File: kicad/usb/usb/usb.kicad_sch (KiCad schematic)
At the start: 17 parts, among them J1 USB_C_Receptacle_USB2.0_14P, J2 PH2.0mm 2P, J3 Conn_01x07_Pin, SW1 PWR, U1 S-T111B33MC-OGSTFU, U2 MCP73831-2-OT

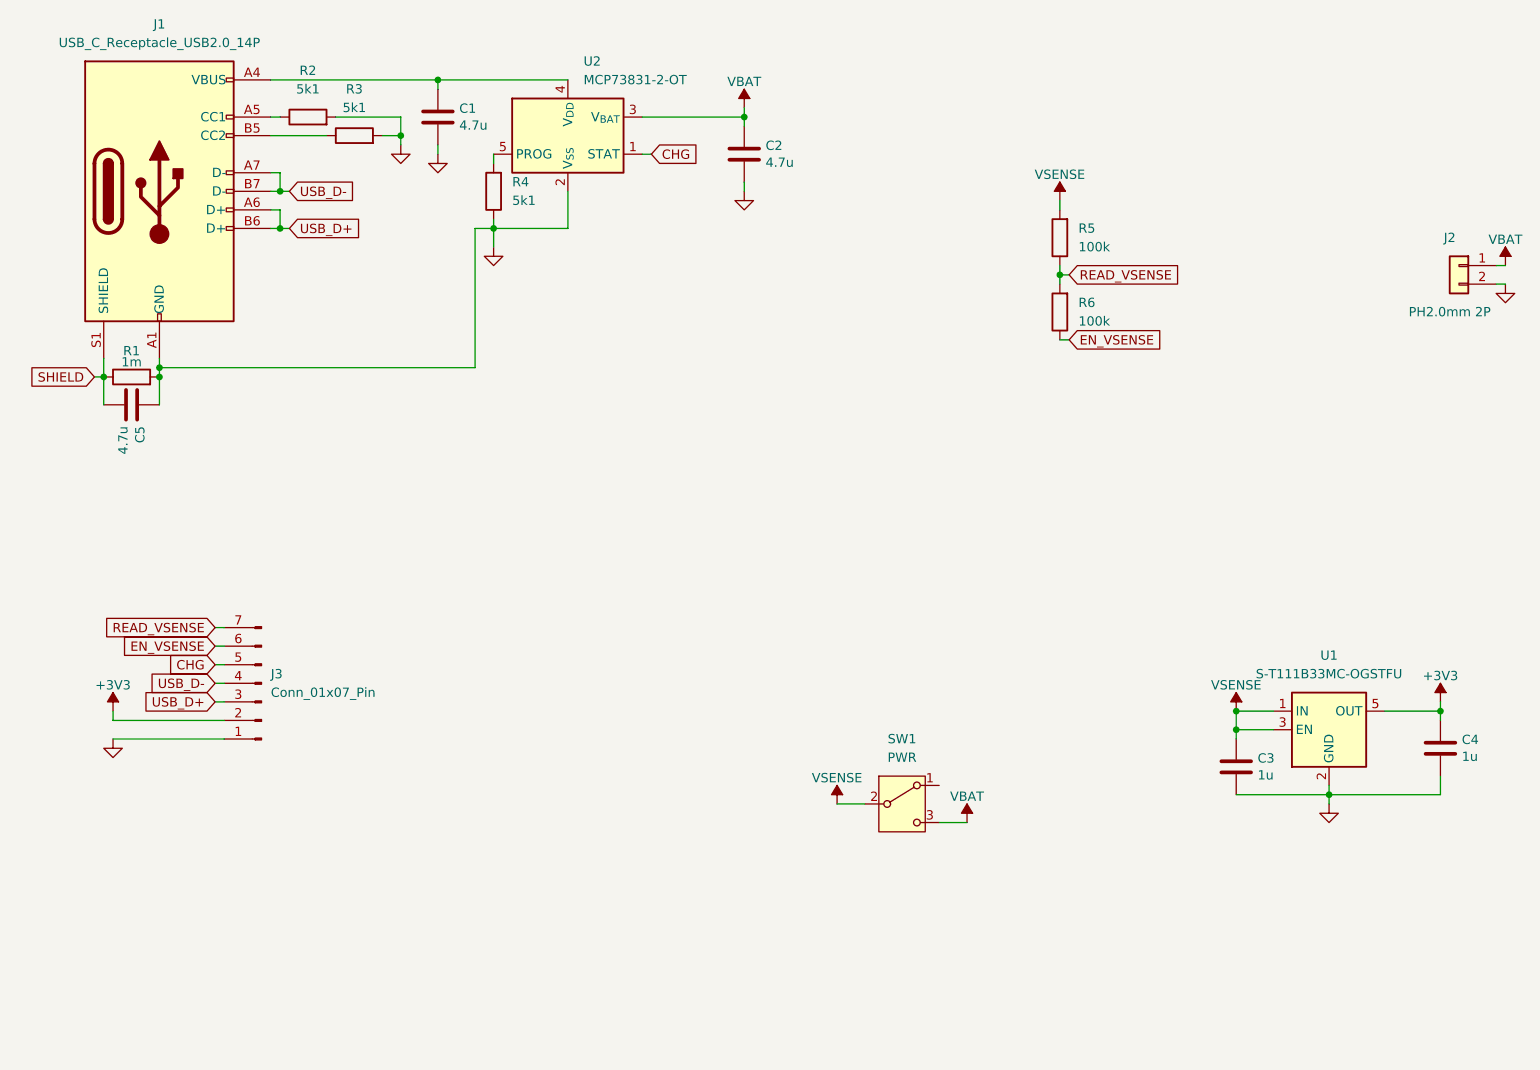
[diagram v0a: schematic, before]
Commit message: Working on usb fabrication
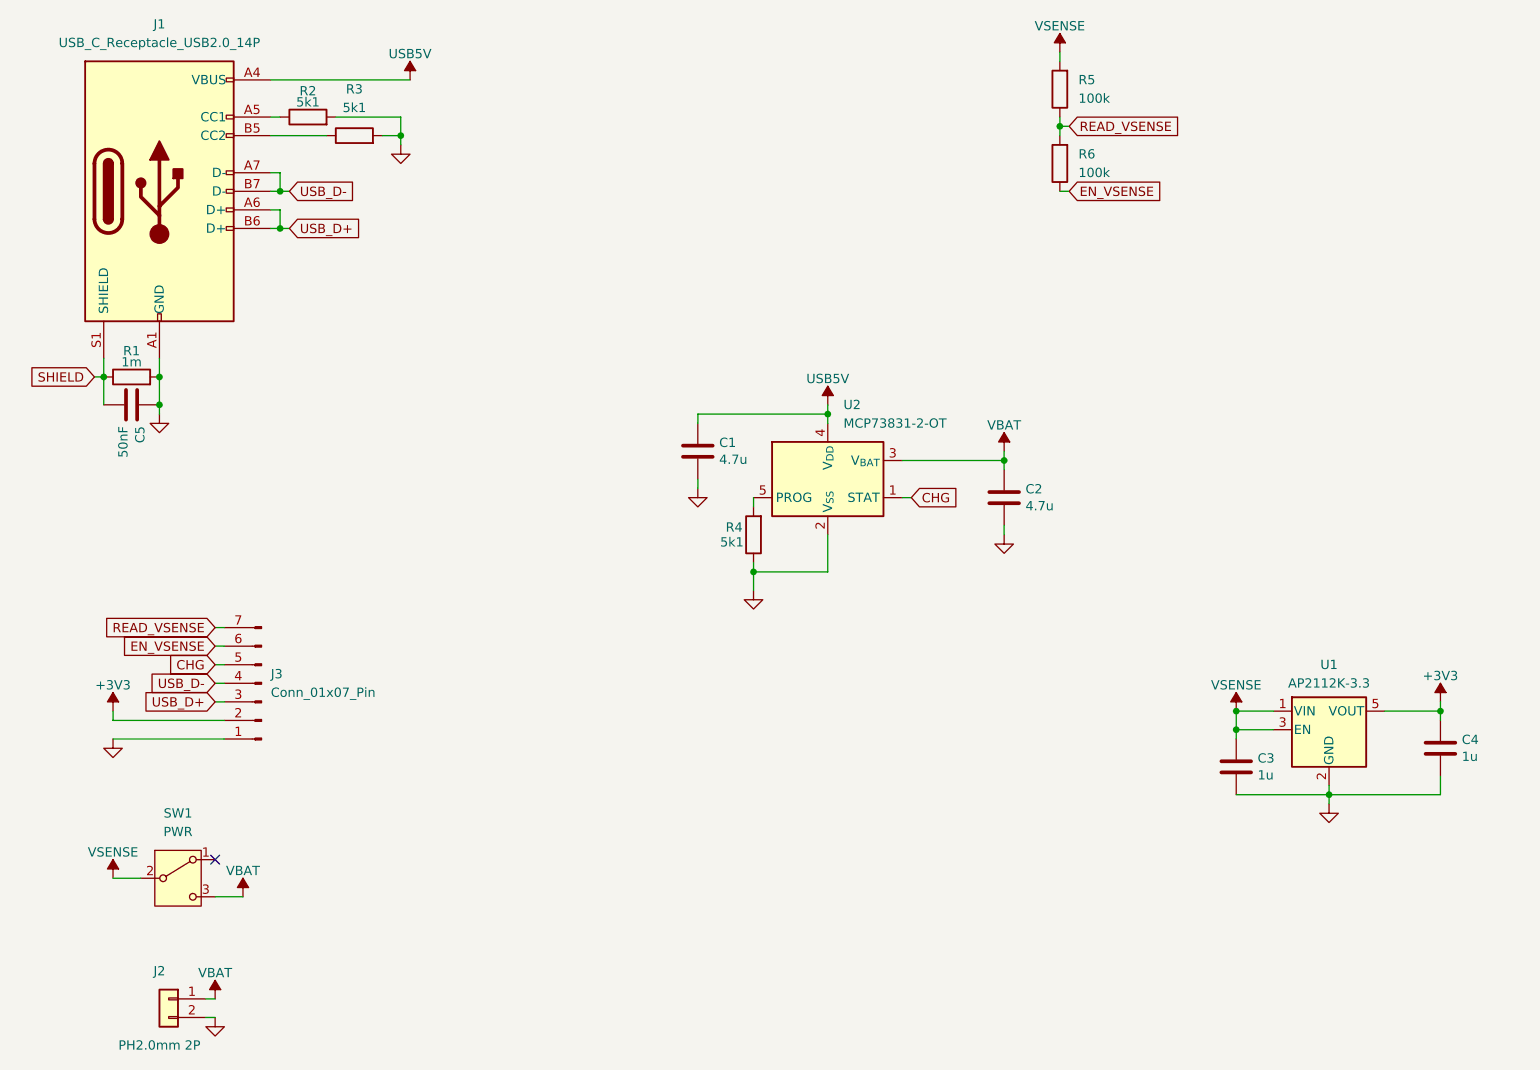
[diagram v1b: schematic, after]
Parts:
- removed U1: S-T111B33MC-OGSTFU, Package_TO_SOT_SMD:SOT-23-5, symbol Regulator_Linear:TPS77012PDBV
- added U1: AP2112K-3.3, Package_TO_SOT_SMD:SOT-23-5, symbol Regulator_Linear:AP2112K-3.3
- C5: value 4.7u -> 50nF; footprint Capacitor_SMD:C_0603_1608Metric_Pad1.08x0.95mm_HandSolder -> Capacitor_SMD:C_0805_2012Metric
- R1: footprint Resistor_SMD:R_0603_1608Metric_Pad0.98x0.95mm_HandSolder -> Resistor_SMD:R_0805_2012Metric
- R2, R3, R4: footprint Resistor_SMD:R_0201_0603Metric_Pad0.64x0.40mm_HandSolder -> Resistor_SMD:R_0805_2012Metric
- R5, R6: footprint Resistor_SMD:R_0402_1005Metric_Pad0.72x0.64mm_HandSolder -> Resistor_SMD:R_0805_2012Metric
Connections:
- net +3V3: now also U1.5 (VOUT)
- net GND: now also U1.2 (GND)
- net VSENSE: now also U1.1 (VIN), U1.3 (EN)
- net USB5V: now reaches C1.1, J1.A4 (VBUS), J1.A9 (VBUS), J1.B4 (VBUS), J1.B9 (VBUS), U2.4 (V_{DD})
- no-connect marks 0 -> 1
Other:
- moved on the sheet: C1, C2, J2, R4, R5, R6, SW1, U2
